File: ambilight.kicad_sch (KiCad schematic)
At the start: 18 parts, among them J1 RGB Connector, J2 USB_C, J3 USB4085-GF-A, U1 ESP-01v090, U2 AZ1117CR-3.3TRG1, U3 FT230XS, U4 AZ1117CR-3.3TRG1

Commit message: Work on USB-C, FT230XS and LDO
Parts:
- removed C1: 100u, Capacitor_THT:C_Rect_L9.0mm_W2.7mm_P7.50mm_MKT, symbol Device:C
- removed C2: 47u, Capacitor_THT:CP_Radial_D12.5mm_P5.00mm, symbol Device:C_Polarized
- removed J2: USB_C, Connector_USB:USB_C_Receptacle_GCT_USB4085, symbol Connector:USB_C_Receptacle_USB2.0_16P
- removed U2: AZ1117CR-3.3TRG1, Package_TO_SOT_SMD:SOT-89-3_Handsoldering, symbol Regulator_Linear:AZ1117-3.3
- added C6: 10uF, symbol Device:C
- added C7: 22uF, symbol Device:C
- added FB1: FerriteBead, symbol Device:FerriteBead
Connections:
- net +3V3: now also C7.1; no longer U3.12 (VCC)
- net GND: now also C6.2, C7.2
- net TXD: now reaches U3.1 (TXD)
- net RXD: now reaches U3.4 (RXD)
- net at J3.A4 (VBUS), J3.A9 (VBUS), J3.B4 (VBUS)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: now also FB1.1; no longer U4.3 (VI)
- new net VCC: C6.1, FB1.2, U3.12 (VCC), U4.3 (VI)
- no-connect marks 14 -> 12
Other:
- note added: "* Should VCCIO and RESET be connected to 3V3OUT/VCC directly when VCC is 3V3? Add TPs to try this? * CBUS1/2 are default RX/TXLED, attach LEDs"
- note added: "LDO"
- note added: "USB-C + UART"
- note removed: "Read datasheet, it says "if VCC is 3V3 then 3V3OUT must also be driven with 3v3 input""
- note removed: "TODO * Caps around U4 * Caps on VBUS (FT230XS datasheet has examples, but seem weird)"
- note removed: "USBDP has internal 1.5k PU"
- moved on the sheet: C3, C4, C5, J1, J3, R1, R2, R3, R4, R5, R6, U3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

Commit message: Use ESP32 instead, add readme
The ESP32 makes a lot more sense in this application. The readme is very
basic and will be used for explaining component choices, among other
things in the future.
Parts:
- removed FB1: FerriteBead, symbol Device:FerriteBead
- removed R1: 3.8R ?, Resistor_THT:R_Axial_DIN0309_L9.0mm_D3.2mm_P2.54mm_Vertical, symbol Device:R
- removed R2: 5R ?, Resistor_THT:R_Axial_DIN0309_L9.0mm_D3.2mm_P2.54mm_Vertical, symbol Device:R
- removed U1: ESP-01v090, ESP8266:ESP-01, symbol ESP8266:ESP-01v090
- removed U3: FT230XS, Package_SO:SSOP-16_3.9x4.9mm_P0.635mm, symbol Interface_USB:FT230XS
- added C1, C2: TBD, symbol Device:C
- added R10, R7, R8, R9: 10kR, symbol Device:R
- added SW1: RESET, symbol Switch:SW_Push
- added SW2: BOOT, symbol Switch:SW_Push
- added U2: ESP32-C3-MINI-1-H4, PCM_Espressif:ESP32-C3-MINI-1, symbol PCM_Espressif:ESP32-C3-MINI-1
- C3: value 100nF -> 0.1uF
- C4: value 47pF -> 10uF
- C5: value 47pF -> 0.1uF
- R3, R4: value 27R -> 0R
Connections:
- net +3V3: now also C4.2, C5.2, R10.1, R7.1, R8.1, R9.1, U2.3 (3V3)
- net GND: now also C4.1, C5.1, SW1.1, SW2.2, U2.1 (GND), U2.11 (GND), U2.14 (GND), U2.2 (GND), U2.36 (GND), U2.37 (GND), U2.38 (GND), U2.39 (GND), U2.40 (GND), U2.41 (GND), U2.42 (GND), U2.43 (GND), U2.44 (GND), U2.45 (GND), U2.46 (GND), U2.47 (GND), U2.48 (GND), U2.49 (GND), U2.50 (GND), U2.51 (GND), U2.52 (GND), U2.53 (GND); no longer C4.2, C5.2
- net VCC: now also J3.A4 (VBUS), J3.A9 (VBUS), J3.B4 (VBUS), J3.B9 (VBUS)
- net USBDP: now reaches J3.A6 (D+), J3.B6 (D+)
- net USBDP: now also R3.2, C1.1; no longer C5.1, R4.1
- net USBDM: now reaches R4.2
- net USBDM: now also J3.A7 (D-), J3.B7 (D-), C2.1
- net at C3.1: now also R7.2, SW1.2, U2.8 (EN/CHIP_PU)
- new net: R9.2, U2.22 (GPIO8)
- new net: R8.2, SW2.1, U2.23 (GPIO9)
- new net: R4.1, U2.26 (GPIO18/USB_D-)
- new net: R3.1, U2.27 (GPIO19/USB_D+)
- new net: R10.2, U2.5 (GPIO2/ADC1_CH2)
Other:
- note added: "ESP32"
- note added: "TODO * Connect RGB connector"
- note added: "USB-C"
- note removed: "* Should VCCIO and RESET be connected to 3V3OUT/VCC directly when VCC is 3V3? Add TPs to try this? * CBUS1/2 are default RX/TXLED, attach LEDs"
- note removed: "USB-C + UART"
- moved on the sheet: J1

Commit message: Bunch of updates and beginning of PCB layout
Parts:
- removed R8, R9: 10kR, symbol Device:R
- added C8: 0.1uF, Capacitor_SMD:C_0805_2012Metric, symbol Device:C
- added C9: 1uF, Capacitor_SMD:C_0805_2012Metric, symbol Device:C
- added D1: LED, LED_SMD:LED_0805_2012Metric, symbol Device:LED
- added J3: Power Connector, Connector_PinHeader_2.54mm:PinHeader_1x03_P2.54mm_Vertical, symbol Connector:Conn_01x03_Pin
- added R3: 120R, Resistor_SMD:R_0805_2012Metric, symbol Device:R
- added R6: 10kR, Resistor_SMD:R_0805_2012Metric, symbol Device:R
- added TP1, TP2, TP3, TP4, TP5: ~, Custom_PCBWay:TestPoint_Pad_D2.5mm_SilkscreenFix, symbol Connector:TestPoint
- added U3: MCP1416, Package_TO_SOT_SMD:SOT-23-5, symbol Driver_FET:MCP1416
- C1: renamed from C6; footprint (none) -> Capacitor_SMD:C_0805_2012Metric
- C2: renamed from C7; footprint (none) -> Capacitor_SMD:C_0805_2012Metric
- C3: footprint (none) -> Capacitor_SMD:C_0805_2012Metric
- C4: value 10uF -> 0.1uF; footprint (none) -> Capacitor_SMD:C_0805_2012Metric
- C5: value 0.1uF -> 10uF; footprint (none) -> Capacitor_SMD:C_0805_2012Metric
- C6: renamed from C1; footprint (none) -> Capacitor_SMD:C_0805_2012Metric
- C7: renamed from C2; footprint (none) -> Capacitor_SMD:C_0805_2012Metric
- J1: renamed from J3; value USB4085-GF-A -> TYPE-C-31-M-12; footprint Connector_USB:USB_C_Receptacle_GCT_USB4085 -> Connector_USB:USB_C_Receptacle_HRO_TYPE-C-31-M-12
- R1: renamed from R6; footprint (none) -> Resistor_SMD:R_0805_2012Metric
- R2: renamed from R5; footprint (none) -> Resistor_SMD:R_0805_2012Metric
- R4: renamed from R7; footprint (none) -> Resistor_SMD:R_0805_2012Metric
- R5: renamed from R10; footprint (none) -> Resistor_SMD:R_0805_2012Metric
- R7: renamed from R3; footprint (none) -> Resistor_SMD:R_0805_2012Metric
- R8: renamed from R4; footprint (none) -> Resistor_SMD:R_0805_2012Metric
- SW1, SW2: footprint (none) -> Button_Switch_SMD:SW_Push_1P1T_NO_CK_KMR2
- renumbered J1 to J2, U4 to U1
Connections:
- net +3V3: now also C4.1, C5.1, R5.2, R3.1, R6.2; no longer C4.2, C5.2, R5.1
- net GND: now also C4.2, C5.2, C6.2, C7.2, J2.1 (Pin_1), C8.2, C9.2, D1.1 (K), J3.1 (Pin_1), U3.4 (GND); no longer C4.1, C5.1
- net VCC: now also J2.3 (Pin_3), C8.1, C9.1, J3.3 (Pin_3), TP1.1, U3.2 (Vdd)
- net at U2.18 (GPIO4/ADC1_CH4): now also TP4.1, U3.3 (IN)
- net at U2.22 (GPIO8): now also R6.1
- net D-: now reaches R8.1, U2.26 (GPIO18/USB_D-)
- net D+: now reaches R7.1, U2.27 (GPIO19/USB_D+)
- net at U2.30 (GPIO20/U0RXD): now also TP3.1
- net at U2.31 (GPIO21/U0TXD): now also TP2.1
- net at U2.5 (GPIO2/ADC1_CH2): now also R5.1; no longer R5.2
- net at J2.2 (Pin_2): now also TP5.1, U3.5 (OUT)
- net USBDM renamed USBD-
- net USBDP renamed USBD+
- new net: D1.2 (A), R3.2
- no-connect marks 12 -> 11
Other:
- note added: "Datasheet talks about ceramic caps, investigate this It also has some layout figures, with lots of vias?"
- note added: "ESP32 + Level Shifter"
- note removed: "ESP32"
- note removed: "TODO * Connect RGB connector"
- moved on the sheet: C1, C2, C3, C6, C7, J1, J2, R1, R2, R4, R5, R7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

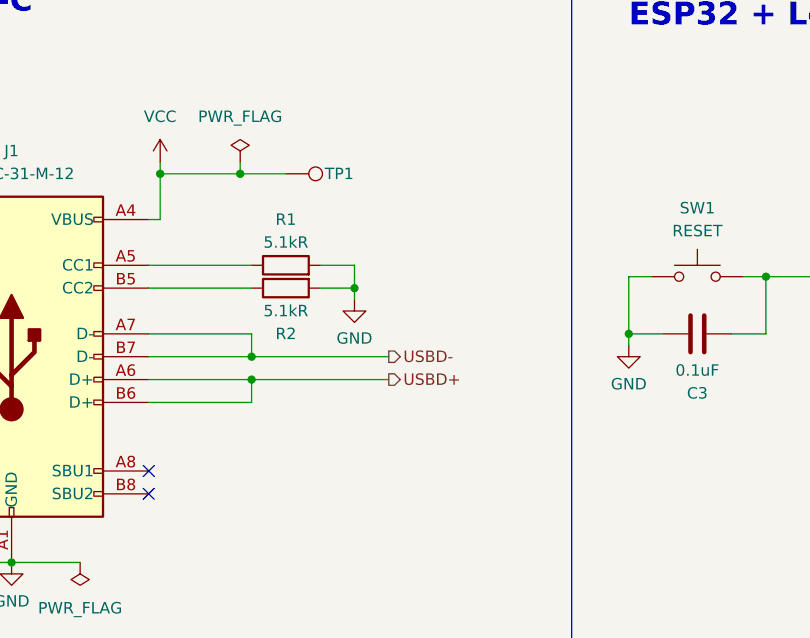
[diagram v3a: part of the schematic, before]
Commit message: Add ESD protection, reroute layout more efficiently
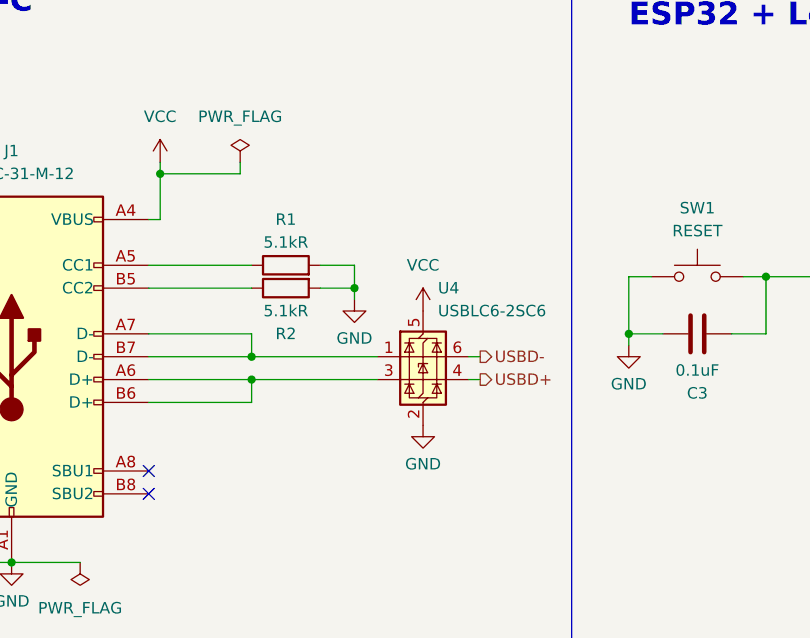
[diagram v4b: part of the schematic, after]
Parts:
- removed TP1: ~, Custom_PCBWay:TestPoint_Pad_D2.5mm_SilkscreenFix, symbol Connector:TestPoint
- added U4: USBLC6-2SC6, Package_TO_SOT_SMD:SOT-23-6, symbol Power_Protection:USBLC6-2SC6
- TP2, TP3, TP4, TP5: footprint Custom_PCBWay:TestPoint_Pad_D2.5mm_SilkscreenFix -> TestPoint:TestPoint_Pad_D1.0mm
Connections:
- net GND: now also U4.2 (GND)
- net USBD+: now also U4.4 (I/O2); no longer J1.A6 (D+), J1.B6 (D+)
- net USBD-: now also U4.6 (I/O1); no longer J1.A7 (D-), J1.B7 (D-)
- net VCC: now also U4.5 (VBUS)
- new net: J1.A7 (D-), J1.B7 (D-), U4.1 (I/O1)
- new net: J1.A6 (D+), J1.B6 (D+), U4.3 (I/O2)
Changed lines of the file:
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@@
 	)
 	(junction
-		(at 52.07 38.1)
-		(diameter 0)
-		(color 0 0 0 0)
-	)
-	(junction
 		(at 40.64 135.89)
 		(diameter 0)
@@
 	(wire
 		(pts
-			(xy 57.15 38.1) (xy 52.07 38.1)
-		)
-		(stroke
-			(width 0)
-			(type default)
-		)
-	)
-	(wire
-		(pts
 			(xy 199.39 90.17) (xy 196.85 90.17)
 		)
@@
 	(wire
 		(pts
-			(xy 53.34 60.96) (xy 68.58 60.96)
+			(xy 53.34 60.96) (xy 67.31 60.96)
 		)
 		(stroke
@@
 	(wire
 		(pts
+			(xy 77.47 60.96) (xy 78.74 60.96)
+		)
+		(stroke
+			(width 0)
+			(type default)
+		)
+	)
+	(wire
+		(pts
 			(xy 41.91 60.96) (xy 53.34 60.96)
 		)
@@
 	(wire
 		(pts
+			(xy 77.47 58.42) (xy 78.74 58.42)
+		)
+		(stroke
+			(width 0)
+			(type default)
+		)
+	)
+	(wire
+		(pts
 			(xy 158.75 26.67) (xy 162.56 26.67)
 		)
@@
 	(wire
 		(pts
-			(xy 53.34 58.42) (xy 68.58 58.42)
+			(xy 53.34 58.42) (xy 67.31 58.42)
 		)
 		(stroke
@@
 	(hierarchical_label "USBD-"
 		(shape output)
-		(at 68.58 58.42 0)
+		(at 78.74 58.42 0)
 		(effects
 			(font
@@
 	(hierarchical_label "USBD+"
 		(shape output)
-		(at 68.58 60.96 0)
+		(at 78.74 60.96 0)
 		(effects
 			(font
@@
 	)
 	(symbol
+		(lib_id "power:VCC")
+		(at 72.39 53.34 0)
+		(unit 1)
+		(exclude_from_sim no)
+		(in_bom yes)
+		(on_board yes)
+		(dnp no)
+		(fields_autoplaced yes)
+		(property "Reference" "#PWR027"
+			(at 72.39 57.15 0)
+			(effects
+				(font
+					(size 1.27 1.27)
+				)
+				(hide yes)
+			)
+		)
+		(property "Value" "VCC"
+			(at 72.39 48.26 0)
+			(effects
+				(font
+					(size 1.27 1.27)
+				)
+			)
+		)
+		(property "Footprint" ""
+			(at 72.39 53.34 0)
+			(effects
+				(font
+					(size 1.27 1.27)
+				)
+				(hide yes)
+			)
+		)
+		(property "Datasheet" ""
+			(at 72.39 53.34 0)
+			(effects
+				(font
+					(size 1.27 1.27)
+				)
+				(hide yes)
+			)
+		)
+		(property "Description" "Power symbol creates a global label with name \"VCC\""
+			(at 72.39 53.34 0)
+			(effects
+				(font
+					(size 1.27 1.27)
+				)
+				(hide yes)
+			)
+		)
+		(pin "1"
+		)
+		(instances
+			(project "ambilight"
+				(path "/3b2736b3-ab99-437a-a7b8-84251aa18a5c"
+					(reference "#PWR027")
+					(unit 1)
+				)
+			)
+		)
+	)
+	(symbol
 		(lib_id "Device:C")
 		(at 175.26 30.48 0)
@@
 			)
 		)
-		(property "Footprint" "Custom_PCBWay:TestPoint_Pad_D2.5mm_SilkscreenFix"
+		(property "Footprint" "TestPoint:TestPoint_Pad_D1.0mm"
 			(at 242.57 80.01 0)
 			(effects
@@
 			)
 		)
-		(property "Footprint" "Custom_PCBWay:TestPoint_Pad_D2.5mm_SilkscreenFix"
+		(property "Footprint" "TestPoint:TestPoint_Pad_D1.0mm"
 			(at 186.69 59.69 0)
 			(effects
@@
 			)
 		)
-		(property "Footprint" "Custom_PCBWay:TestPoint_Pad_D2.5mm_SilkscreenFix"
+		(property "Footprint" "TestPoint:TestPoint_Pad_D1.0mm"
 			(at 209.55 80.01 0)
 			(effects
@@
 			)
 		)
-		(property "Footprint" "Custom_PCBWay:TestPoint_Pad_D2.5mm_SilkscreenFix"
+		(property "Footprint" "TestPoint:TestPoint_Pad_D1.0mm"
 			(at 186.69 62.23 0)
 			(effects
@@
 	)
 	(symbol
+		(lib_id "power:GND")
+		(at 72.39 66.04 0)
+		(unit 1)
+		(exclude_from_sim no)
+		(in_bom yes)
+		(on_board yes)
+		(dnp no)
+		(property "Reference" "#PWR026"
+			(at 72.39 72.39 0)
+			(effects
+				(font
+					(size 1.27 1.27)
+				)
+				(hide yes)
+			)
+		)
+		(property "Value" "GND"
+			(at 72.39 70.358 0)
+			(effects
+				(font
+					(size 1.27 1.27)
+				)
+			)
+		)
+		(property "Footprint" ""
+			(at 72.39 66.04 0)
+			(effects
+				(font
+					(size 1.27 1.27)
+				)
+				(hide yes)
+			)
+		)
+		(property "Datasheet" ""
+			(at 72.39 66.04 0)
+			(effects
+				(font
+					(size 1.27 1.27)
+				)
+				(hide yes)
+			)
+		)
+		(property "Description" "Power symbol creates a global label with name \"GND\" , ground"
+			(at 72.39 66.04 0)
+			(effects
+				(font
+					(size 1.27 1.27)
+				)
+				(hide yes)
+			)
+		)
+		(pin "1"
+		)
+		(instances
+			(project "ambilight"
+				(path "/3b2736b3-ab99-437a-a7b8-84251aa18a5c"
+					(reference "#PWR026")
+					(unit 1)
+				)
+			)
+		)
+	)
+	(symbol
 		(lib_id "Regulator_Linear:AZ1117-3.3")
 		(at 40.64 127 0)
@@
 	)
 	(symbol
-		(lib_id "Device:R")
-		(at 57.15 50.8 90)
-		(mirror x)
+		(lib_id "Power_Protection:USBLC6-2SC6")
+		(at 72.39 58.42 0)
 		(unit 1)
 		(exclude_from_sim no)
@@
 		(on_board yes)
 		(dnp no)
-		(property "Reference" "R2"
-			(at 57.15 55.88 90)
+		(fields_autoplaced yes)
+		(property "Reference" "U4"
+			(at 74.0411 50.8 0)
 			(effects
 				(font
 					(size 1.27 1.27)
 				)
+				(justify left)
 			)
 		)
-		(property "Value" "5.1kR"
-			(at 57.15 53.34 90)
+		(property "Value" "USBLC6-2SC6"
+			(at 74.0411 53.34 0)
 			(effects
 				(font
 					(size 1.27 1.27)
 				)
+				(justify left)
 			)
 		)
-		(property "Footprint" "Resistor_SMD:R_0805_2012Metric"
-			(at 57.15 49.022 90)
+		(property "Footprint" "Package_TO_SOT_SMD:SOT-23-6"
+			(at 73.66 64.77 0)
 			(effects
 				(font
 					(size 1.27 1.27)
+					(italic yes)
 				)
+				(justify left)
 				(hide yes)
 			)
 		)
-		(property "Datasheet" "~"
-			(at 57.15 50.8 0)
+		(property "Datasheet" "https://www.st.com/resource/en/datasheet/usblc6-2.pdf"
+			(at 73.66 66.675 0)
 			(effects
 				(font
 					(size 1.27 1.27)
 				)
+				(justify left)
 				(hide yes)
 			)
 		)
-		(property "Description" "Resistor"
-			(at 57.15 50.8 0)
+		(property "Description" "Very low capacitance ESD protection diode, 2 data-line, SOT-23-6"
+			(at 72.39 58.42 0)
 			(effects
 				(font
@@
 			)
 		)
+		(pin "1"
+		)
+		(pin "3"
+		)
 		(pin "2"
 		)
-		(pin "1"
+		(pin "6"
+		)
+		(pin "5"
+		)
+		(pin "4"
 		)
 		(instances
-			(project "ambilight"
+			(project ""
 				(path "/3b2736b3-ab99-437a-a7b8-84251aa18a5c"
-					(reference "R2")
+					(reference "U4")
 					(unit 1)
 				)
@@
 	)
 	(symbol
-		(lib_id "Connector:TestPoint")
-		(at 57.15 38.1 270)
+		(lib_id "Device:R")
+		(at 57.15 50.8 90)
+		(mirror x)
 		(unit 1)
 		(exclude_from_sim no)
@@
 		(on_board yes)
 		(dnp no)
-		(property "Reference" "TP1"
-			(at 61.468 38.1 90)
+		(property "Reference" "R2"
+			(at 57.15 55.88 90)
 			(effects
 				(font
 					(size 1.27 1.27)
 				)
-				(justify left)
 			)
 		)
-		(property "Value" "~"
-			(at 62.23 39.37 90)
+		(property "Value" "5.1kR"
+			(at 57.15 53.34 90)
 			(effects
 				(font
 					(size 1.27 1.27)
 				)
-				(justify left)
 			)
 		)
-		(property "Footprint" "Custom_PCBWay:TestPoint_Pad_D2.5mm_SilkscreenFix"
-			(at 57.15 43.18 0)
+		(property "Footprint" "Resistor_SMD:R_0805_2012Metric"
+			(at 57.15 49.022 90)
 			(effects
 				(font
@@
 		)
 		(property "Datasheet" "~"
-			(at 57.15 43.18 0)
+			(at 57.15 50.8 0)
 			(effects
 				(font
@@
 			)
 		)
-		(property "Description" "test point"
-			(at 57.15 38.1 0)
+		(property "Description" "Resistor"
+			(at 57.15 50.8 0)
 			(effects
 				(font
@@
 			)
 		)
+		(pin "2"
+		)
 		(pin "1"
 		)
 		(instances
-			(project ""
+			(project "ambilight"
 				(path "/3b2736b3-ab99-437a-a7b8-84251aa18a5c"
-					(reference "TP1")
+					(reference "R2")
 					(unit 1)
 				)

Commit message: Minor layout adjustments
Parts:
- TP2, TP3, TP4, TP5: footprint TestPoint:TestPoint_Pad_D1.0mm -> Custom_PCBWay:TestPoint_Pad_D1.0mm_SilkscreenFix
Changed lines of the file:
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@@
 			)
 		)
-		(property "Footprint" "TestPoint:TestPoint_Pad_D1.0mm"
+		(property "Footprint" "Custom_PCBWay:TestPoint_Pad_D1.0mm_SilkscreenFix"
 			(at 242.57 80.01 0)
 			(effects
@@
 			)
 		)
-		(property "Footprint" "TestPoint:TestPoint_Pad_D1.0mm"
+		(property "Footprint" "Custom_PCBWay:TestPoint_Pad_D1.0mm_SilkscreenFix"
 			(at 186.69 59.69 0)
 			(effects
@@
 			)
 		)
-		(property "Footprint" "TestPoint:TestPoint_Pad_D1.0mm"
+		(property "Footprint" "Custom_PCBWay:TestPoint_Pad_D1.0mm_SilkscreenFix"
 			(at 209.55 80.01 0)
 			(effects
@@
 			)
 		)
-		(property "Footprint" "TestPoint:TestPoint_Pad_D1.0mm"
+		(property "Footprint" "Custom_PCBWay:TestPoint_Pad_D1.0mm_SilkscreenFix"
 			(at 186.69 62.23 0)
 			(effects
